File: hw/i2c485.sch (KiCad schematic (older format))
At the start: 31 parts, among them IC1 ATMEGA328-A, IC2 SP3485CN, P1 CONN_4, P2 CONN_4, P3 CONN_3X2, U1 78L05, X1 3,6864MHz

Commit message: led
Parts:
- added D7, D8: LED, ~, symbol LED
- added R8: 470R, ~, symbol R
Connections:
- net GND: now also D7.2 (K), D8.2 (K)
- net LED: now reaches IC1.24 ((PCINT9/ADC1)PC1)
- net LED: now also R8.2
- new net: D7.1 (A), D8.1 (A), R8.1
- no-connect marks 14 -> 13
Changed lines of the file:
@@
 	1    0    0    -1
 $EndComp
-NoConn ~ 5850 2600
 NoConn ~ 5850 2700
 NoConn ~ 5850 2800
 NoConn ~ 5850 3450
-NoConn ~ 5850 3550
 NoConn ~ 5850 3650
 NoConn ~ 5850 3750
@@
 Wire Wire Line
 	2400 3050 2200 3050
+$Comp
+L LED D7
+U 1 1 53D0F49F
+P 4000 1700
+F 0 "D7" H 4000 1800 50  0000 C CNN
+F 1 "LED" H 4000 1600 50  0000 C CNN
+F 2 "~" H 4000 1700 60  0000 C CNN
+F 3 "~" H 4000 1700 60  0000 C CNN
+	1    4000 1700
+	-1   0    0    1
+$EndComp
+$Comp
+L R R8
+U 1 1 53D0F4AC
+P 4650 1700
+F 0 "R8" V 4730 1700 40  0000 C CNN
+F 1 "470R" V 4657 1701 40  0000 C CNN
+F 2 "~" V 4580 1700 30  0000 C CNN
+F 3 "~" H 4650 1700 30  0000 C CNN
+	1    4650 1700
+	0    -1   -1   0
+$EndComp
+Text GLabel 4900 1700 2    60   Input ~ 0
+LED
+$Comp
+L GND #PWR033
+U 1 1 53D0F4B4
+P 3700 1800
+F 0 "#PWR033" H 3700 1800 30  0001 C CNN
+F 1 "GND" H 3700 1730 30  0001 C CNN
+F 2 "" H 3700 1800 60  0000 C CNN
+F 3 "" H 3700 1800 60  0000 C CNN
+	1    3700 1800
+	1    0    0    -1
+$EndComp
+Wire Wire Line
+	3700 1400 3700 1800
+Wire Wire Line
+	3700 1700 3800 1700
+Text GLabel 6000 3550 2    60   Input ~ 0
+LED
+Wire Wire Line
+	6000 3550 5850 3550
+NoConn ~ 5850 2600
+$Comp
+L LED D8
+U 1 1 53D0F700
+P 4000 1400
+F 0 "D8" H 4000 1500 50  0000 C CNN
+F 1 "LED" H 4000 1300 50  0000 C CNN
+F 2 "~" H 4000 1400 60  0000 C CNN
+F 3 "~" H 4000 1400 60  0000 C CNN
+	1    4000 1400
+	-1   0    0    1
+$EndComp
+Wire Wire Line
+	4200 1700 4400 1700
+Wire Wire Line
+	4200 1400 4300 1400
+Wire Wire Line
+	4300 1400 4300 1700
+Connection ~ 4300 1700
+Wire Wire Line
+	3700 1400 3800 1400
+Connection ~ 3700 1700
 $EndSCHEMATC

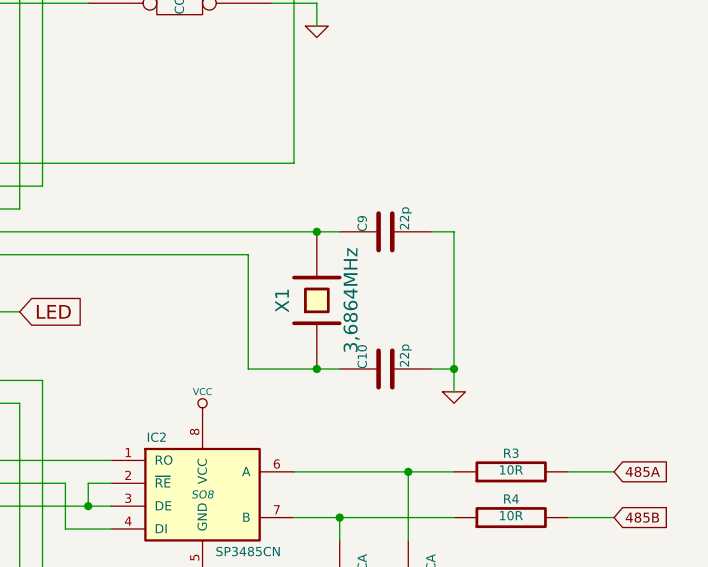
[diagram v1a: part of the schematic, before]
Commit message: crystal load cap. value
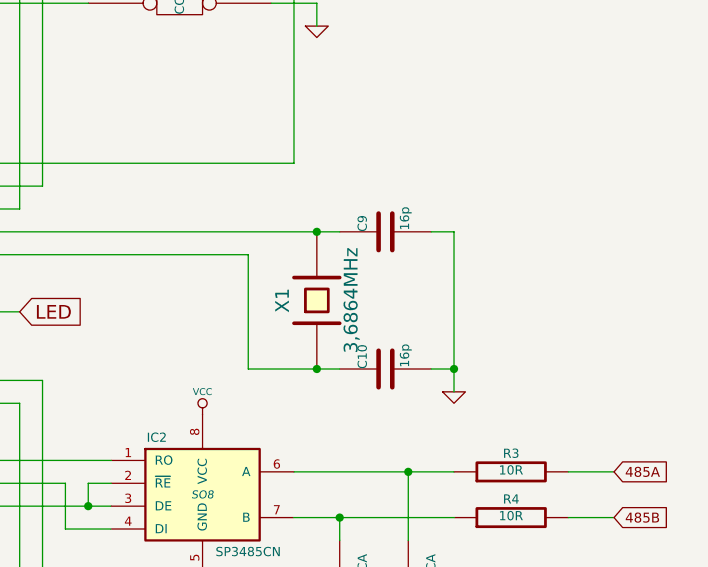
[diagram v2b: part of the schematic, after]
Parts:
- C10, C9: value 22p -> 16p
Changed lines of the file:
@@
 Sheet 1 1
 Title ""
-Date "24 jul 2014"
+Date "21 aug 2014"
 Rev ""
 Comp ""
@@
 P 7600 3200
 F 0 "C9" H 7600 3300 40  0000 L CNN
-F 1 "22p" H 7606 3115 40  0000 L CNN
+F 1 "16p" H 7606 3115 40  0000 L CNN
 F 2 "~" H 7638 3050 30  0000 C CNN
 F 3 "~" H 7600 3200 60  0000 C CNN
@@
 P 7600 3800
 F 0 "C10" H 7600 3900 40  0000 L CNN
-F 1 "22p" H 7606 3715 40  0000 L CNN
+F 1 "16p" H 7606 3715 40  0000 L CNN
 F 2 "~" H 7638 3650 30  0000 C CNN
 F 3 "~" H 7600 3800 60  0000 C CNN
